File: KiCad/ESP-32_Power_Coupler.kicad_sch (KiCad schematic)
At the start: 5 parts

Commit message: very rough sketch layout
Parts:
- C11: renamed from C2; footprint (none) -> Capacitor_SMD:C_0402_1005Metric
- C12: renamed from C5; footprint (none) -> Capacitor_SMD:C_0402_1005Metric
- C13: renamed from C6; footprint (none) -> Capacitor_SMD:C_0402_1005Metric
- C14: renamed from C7; footprint (none) -> Capacitor_SMD:C_0603_1608Metric
- L1: footprint (none) -> Inductor_SMD:L_0402_1005Metric
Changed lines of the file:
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@@
 		(dnp no)
 		(fields_autoplaced yes)
-		(property "Reference" "#PWR012"
+		(property "Reference" "#PWR024"
 			(at 175.26 71.12 0)
 			(effects
@@
 			(project ""
 				(path "/16f8cce7-467e-4342-b55a-00af81cd6f69/fc885ce6-a9ef-46cc-bb26-b706458b9a56"
-					(reference "#PWR012")
+					(reference "#PWR024")
 					(unit 1)
 				)
@@
 		(dnp no)
 		(fields_autoplaced yes)
-		(property "Reference" "#PWR013"
+		(property "Reference" "#PWR025"
 			(at 185.42 71.12 0)
 			(effects
@@
 			(project ""
 				(path "/16f8cce7-467e-4342-b55a-00af81cd6f69/fc885ce6-a9ef-46cc-bb26-b706458b9a56"
-					(reference "#PWR013")
+					(reference "#PWR025")
 					(unit 1)
 				)
@@
 			)
 		)
-		(property "Footprint" ""
+		(property "Footprint" "Inductor_SMD:L_0402_1005Metric"
 			(at 180.34 49.53 0)
 			(effects
@@
 		(dnp no)
 		(fields_autoplaced yes)
-		(property "Reference" "C7"
+		(property "Reference" "C14"
 			(at 209.55 57.1499 0)
 			(effects
@@
 			)
 		)
-		(property "Footprint" ""
+		(property "Footprint" "Capacitor_SMD:C_0603_1608Metric"
 			(at 206.7052 62.23 0)
 			(effects
@@
 			(project "Senior Project"
 				(path "/16f8cce7-467e-4342-b55a-00af81cd6f69/fc885ce6-a9ef-46cc-bb26-b706458b9a56"
-					(reference "C7")
+					(reference "C14")
 					(unit 1)
 				)
@@
 		(dnp no)
 		(fields_autoplaced yes)
-		(property "Reference" "#PWR015"
+		(property "Reference" "#PWR028"
 			(at 205.74 71.12 0)
 			(effects
@@
 			(project ""
 				(path "/16f8cce7-467e-4342-b55a-00af81cd6f69/fc885ce6-a9ef-46cc-bb26-b706458b9a56"
-					(reference "#PWR015")
+					(reference "#PWR028")
 					(unit 1)
 				)
@@
 		(dnp no)
 		(fields_autoplaced yes)
-		(property "Reference" "C6"
+		(property "Reference" "C13"
 			(at 199.39 57.1499 0)
 			(effects
@@
 			)
 		)
-		(property "Footprint" ""
+		(property "Footprint" "Capacitor_SMD:C_0402_1005Metric"
 			(at 196.5452 62.23 0)
 			(effects
@@
 			(project "Senior Project"
 				(path "/16f8cce7-467e-4342-b55a-00af81cd6f69/fc885ce6-a9ef-46cc-bb26-b706458b9a56"
-					(reference "C6")
+					(reference "C13")
 					(unit 1)
 				)
@@
 		(dnp no)
 		(fields_autoplaced yes)
-		(property "Reference" "#PWR020"
+		(property "Reference" "#PWR027"
 			(at 205.74 50.8 0)
 			(effects
@@
 			(project ""
 				(path "/16f8cce7-467e-4342-b55a-00af81cd6f69/fc885ce6-a9ef-46cc-bb26-b706458b9a56"
-					(reference "#PWR020")
+					(reference "#PWR027")
 					(unit 1)
 				)
@@
 		(dnp no)
 		(fields_autoplaced yes)
-		(property "Reference" "C2"
+		(property "Reference" "C11"
 			(at 179.07 57.1499 0)
 			(effects
@@
 			)
 		)
-		(property "Footprint" ""
+		(property "Footprint" "Capacitor_SMD:C_0402_1005Metric"
 			(at 176.2252 62.23 0)
 			(effects
@@
 			(project ""
 				(path "/16f8cce7-467e-4342-b55a-00af81cd6f69/fc885ce6-a9ef-46cc-bb26-b706458b9a56"
-					(reference "C2")
+					(reference "C11")
 					(unit 1)
 				)
@@
 		(dnp no)
 		(fields_autoplaced yes)
-		(property "Reference" "#PWR014"
+		(property "Reference" "#PWR026"
 			(at 195.58 71.12 0)
 			(effects
@@
 			(project ""
 				(path "/16f8cce7-467e-4342-b55a-00af81cd6f69/fc885ce6-a9ef-46cc-bb26-b706458b9a56"
-					(reference "#PWR014")
+					(reference "#PWR026")
 					(unit 1)
 				)
@@
 		(dnp no)
 		(fields_autoplaced yes)
-		(property "Reference" "C5"
+		(property "Reference" "C12"
 			(at 189.23 57.1499 0)
 			(effects
@@
 			)
 		)
-		(property "Footprint" ""
+		(property "Footprint" "Capacitor_SMD:C_0402_1005Metric"
 			(at 186.3852 62.23 0)
 			(effects
@@
 			(project "Senior Project"
 				(path "/16f8cce7-467e-4342-b55a-00af81cd6f69/fc885ce6-a9ef-46cc-bb26-b706458b9a56"
-					(reference "C5")
-					(unit 1)
-				)
+					(reference "C12")
+					(unit 1)
+				)

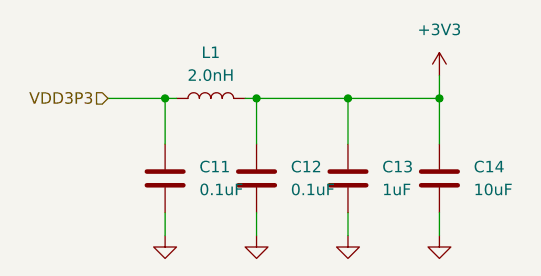
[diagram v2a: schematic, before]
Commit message: tighten up layout, swap out USB connector
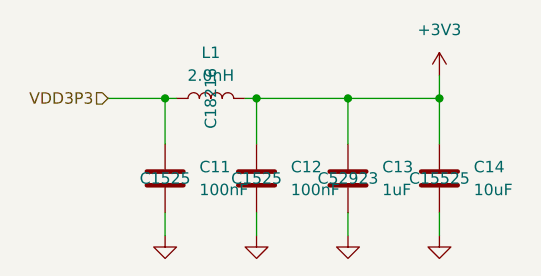
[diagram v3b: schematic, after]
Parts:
- C11, C12: value 0.1uF -> 100nF; LCSC (none) -> C1525
- C13: LCSC (none) -> C52923
- C14: footprint Capacitor_SMD:C_0603_1608Metric -> Capacitor_SMD:C_0402_1005Metric; LCSC (none) -> C15525
- L1: LCSC (none) -> C18216
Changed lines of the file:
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@@
+			)
+		)
+		(property "LCSC" "C18216"
+			(at 180.34 49.53 0)
+			(effects
+				(font
+					(size 1.27 1.27)
+				)
 			)
 		)
@@
 			)
 		)
-		(property "Footprint" "Capacitor_SMD:C_0603_1608Metric"
+		(property "Footprint" "Capacitor_SMD:C_0402_1005Metric"
 			(at 206.7052 62.23 0)
 			(effects
@@
 			)
 		)
+		(property "LCSC" "C15525"
+			(at 205.74 58.42 0)
+			(effects
+				(font
+					(size 1.27 1.27)
+				)
+			)
+		)
 		(pin "1"
 		)
@@
 			)
 		)
+		(property "LCSC" "C52923"
+			(at 195.58 58.42 0)
+			(effects
+				(font
+					(size 1.27 1.27)
+				)
+			)
+		)
 		(pin "1"
 		)
@@
 			)
 		)
-		(property "Value" "0.1uF"
+		(property "Value" "100nF"
 			(at 179.07 59.6899 0)
 			(effects
@@
 			)
 		)
+		(property "LCSC" "C1525"
+			(at 175.26 58.42 0)
+			(effects
+				(font
+					(size 1.27 1.27)
+				)
+			)
+		)
 		(pin "1"
 		)
@@
 			)
 		)
-		(property "Value" "0.1uF"
+		(property "Value" "100nF"
 			(at 189.23 59.6899 0)
 			(effects
@@
 			)
 		)
+		(property "LCSC" "C1525"
+			(at 185.42 58.42 0)
+			(effects
+				(font
+					(size 1.27 1.27)
+				)
+			)
+		)
